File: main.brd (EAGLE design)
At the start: 24.5 x 25.1 mm, 35 parts, among them IC1 ATTINY13A-SSH, IC2 TP4056-42-ESOP8, IC3 LM27313XMFX_NOPB, T1A 2N4401, T1B NPN, X1 MINI-USB-UX60A-MB-5ST

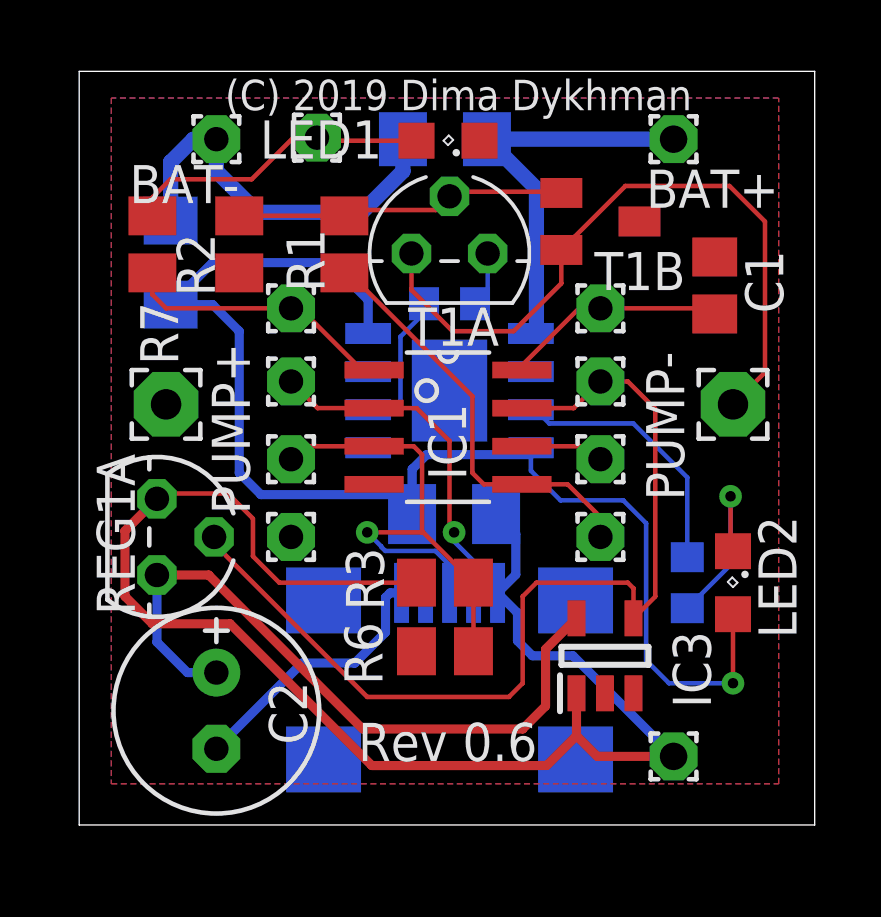
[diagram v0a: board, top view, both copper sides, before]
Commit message: solar parameters tuned
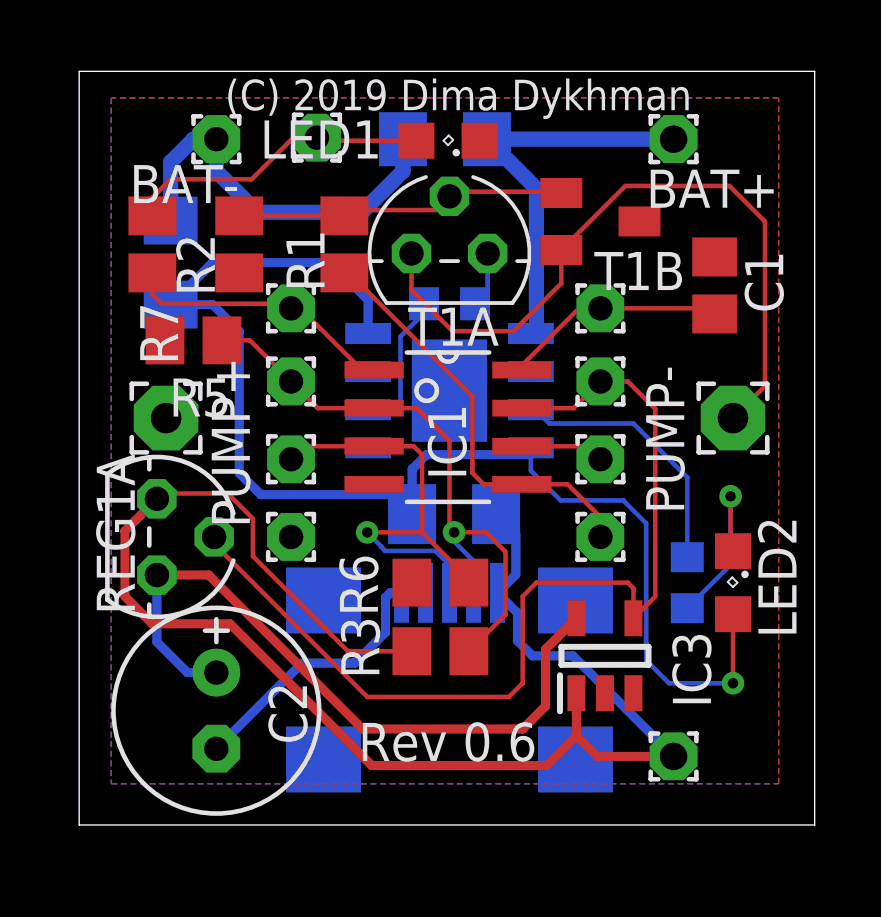
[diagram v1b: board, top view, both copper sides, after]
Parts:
- added R5: 10k, resistor:M0805
- moved R3 2.29 mm to (13.0, 5.94)
- moved R6 2.29 mm to (13.0, 8.23)
- moved PUMP+ 0.46 mm to (3.81, 13.7)
- moved PUMP- 0.46 mm to (22.7, 13.7)
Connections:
- net GND: now also R5.2
- net SENSOR-: no longer R3.1
- net UART_TX: now also R3.1, R5.1
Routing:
- net UART_TX: track 11.5 -> 20.2 mm
- net SENSOR-: track 17.9 -> 15.5 mm
- net N$3: track 48.9 -> 49.7 mm
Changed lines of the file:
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@@
 <attribute name="VALUE" x="8.7884" y="18.2372" size="1.27" layer="27" rot="R90"/>
 </element>
-<element name="PUMP-" library="wirepad" library_urn="urn:adsk.eagle:library:412" package="2,15/1,0" package3d_urn="urn:adsk.eagle:package:30831/1" value="" x="22.7076" y="14.1732" smashed="yes" rot="R90">
-<attribute name="NAME" x="21.082" y="10.9728" size="1.27" layer="25" ratio="10" rot="R90"/>
-<attribute name="VALUE" x="22.1076" y="14.1732" size="0.0254" layer="27" rot="R90"/>
-</element>
-<element name="PUMP+" library="wirepad" library_urn="urn:adsk.eagle:library:412" package="2,15/1,0" package3d_urn="urn:adsk.eagle:package:30831/1" value="" x="3.81" y="14.1732" smashed="yes" rot="R90">
-<attribute name="NAME" x="6.604" y="10.5156" size="1.27" layer="25" ratio="10" rot="R90"/>
-<attribute name="VALUE" x="3.21" y="14.1732" size="0.0254" layer="27" rot="R90"/>
+<element name="PUMP-" library="wirepad" library_urn="urn:adsk.eagle:library:412" package="2,15/1,0" package3d_urn="urn:adsk.eagle:package:30831/1" value="" x="22.7076" y="13.716" smashed="yes" rot="R90">
+<attribute name="NAME" x="21.082" y="10.5156" size="1.27" layer="25" ratio="10" rot="R90"/>
+<attribute name="VALUE" x="22.1076" y="13.716" size="0.0254" layer="27" rot="R90"/>
+</element>
+<element name="PUMP+" library="wirepad" library_urn="urn:adsk.eagle:library:412" package="2,15/1,0" package3d_urn="urn:adsk.eagle:package:30831/1" value="" x="3.81" y="13.716" smashed="yes" rot="R90">
+<attribute name="NAME" x="6.604" y="10.0584" size="1.27" layer="25" ratio="10" rot="R90"/>
+<attribute name="VALUE" x="3.21" y="13.716" size="0.0254" layer="27" rot="R90"/>
 </element>
 <element name="PAD1" library="wirepad" library_urn="urn:adsk.eagle:library:412" package="1,6/0,8" package3d_urn="urn:adsk.eagle:package:30830/1" value="" x="8.8392" y="23.0632" smashed="yes">
@@
 <attribute name="VALUE" x="2.2352" y="6.8326" size="1.27" layer="27" ratio="10" rot="R270"/>
 </element>
-<element name="R6" library="resistor" library_urn="urn:adsk.eagle:library:348" package="M0805" package3d_urn="urn:adsk.eagle:package:23556/1" value="10k" x="13.1064" y="5.9436" smashed="yes" rot="R180">
-<attribute name="NAME" x="11.0236" y="4.826" size="1.27" layer="25" rot="R90"/>
-<attribute name="VALUE" x="14.3764" y="8.4836" size="1.27" layer="27" rot="R180"/>
+<element name="R6" library="resistor" library_urn="urn:adsk.eagle:library:348" package="M0805" package3d_urn="urn:adsk.eagle:package:23556/1" value="10k" x="12.954" y="8.2296" smashed="yes" rot="R180">
+<attribute name="NAME" x="10.8712" y="7.112" size="1.27" layer="25" rot="R90"/>
+<attribute name="VALUE" x="14.224" y="10.7696" size="1.27" layer="27" rot="R180"/>
 </element>
 <element name="C1" library="rcl" library_urn="urn:adsk.eagle:library:334" package="C0805" package3d_urn="urn:adsk.eagle:package:23617/2" value="100nF" x="22.098" y="18.1356" smashed="yes" rot="R90">
@@
 <attribute name="VALUE" x="24.638" y="16.8656" size="1.27" layer="27" rot="R90"/>
 </element>
-<element name="R3" library="resistor" library_urn="urn:adsk.eagle:library:348" package="M0805" package3d_urn="urn:adsk.eagle:package:23556/1" value="10k" x="13.1064" y="8.2296" smashed="yes" rot="R180">
-<attribute name="NAME" x="9.8044" y="9.398" size="1.27" layer="25" rot="R270"/>
-<attribute name="VALUE" x="14.3764" y="10.7696" size="1.27" layer="27" rot="R180"/>
+<element name="R3" library="resistor" library_urn="urn:adsk.eagle:library:348" package="M0805" package3d_urn="urn:adsk.eagle:package:23556/1" value="10k" x="12.954" y="5.9436" smashed="yes" rot="R180">
+<attribute name="NAME" x="9.652" y="7.112" size="1.27" layer="25" rot="R270"/>
+<attribute name="VALUE" x="14.224" y="8.4836" size="1.27" layer="27" rot="R180"/>
 </element>
 <element name="R7" library="resistor" library_urn="urn:adsk.eagle:library:348" package="M0805" package3d_urn="urn:adsk.eagle:package:23556/1" value="510" x="3.3528" y="19.5072" smashed="yes" rot="R90">
@@
 <attribute name="RS_PRICE-STOCK" value="" x="18.4404" y="5.7912" size="1.778" layer="27" rot="R90" display="off"/>
 <attribute name="VALUE" x="18.4404" y="5.7912" size="1.27" layer="27" rot="R90" align="center"/>
+</element>
+<element name="R5" library="resistor" library_urn="urn:adsk.eagle:library:348" package="M0805" package3d_urn="urn:adsk.eagle:package:23556/1" value="10k" x="4.7244" y="16.3068" smashed="yes" rot="R180">
+<attribute name="NAME" x="5.9944" y="15.0368" size="1.27" layer="25" rot="R180"/>
+<attribute name="VALUE" x="5.9944" y="18.8468" size="1.27" layer="27" rot="R180"/>
 </element>
 </elements>
@@
 <contactref element="X1" pad="2"/>
 <wire x1="14.0588" y1="8.9536" x2="14.0588" y2="7.8888" width="0.1524" layer="16"/>
+<contactref element="R5" pad="1"/>
+<contactref element="R3" pad="1"/>
+<wire x1="5.6744" y1="16.3068" x2="6.604" y2="16.3068" width="0.1524" layer="1"/>
+<wire x1="6.604" y1="16.3068" x2="7.9756" y2="14.9352" width="0.1524" layer="1"/>
+<wire x1="15.1232" y1="9.2608" x2="14.478" y2="9.906" width="0.1524" layer="1"/>
+<wire x1="13.4112" y1="9.906" x2="14.478" y2="9.906" width="0.1524" layer="1"/>
+<wire x1="15.1232" y1="9.2608" x2="15.1232" y2="7.1628" width="0.1524" layer="1"/>
+<wire x1="15.1232" y1="7.1628" x2="13.904" y2="5.9436" width="0.1524" layer="1"/>
 </signal>
 <signal name="GND">
@@
 <wire x1="8.3422" y1="5.5482" x2="5.4864" y2="2.6924" width="0.3048" layer="16"/>
 <contactref element="IC3" pad="2"/>
+<contactref element="R5" pad="2"/>
 </signal>
 <signal name="N$1">
@@
 <contactref element="T1B" pad="2"/>
 <contactref element="PUMP-" pad="1"/>
-<wire x1="22.7076" y1="14.1732" x2="23.7744" y2="15.24" width="0.1524" layer="1"/>
-<wire x1="23.7744" y1="15.24" x2="23.7744" y2="20.2692" width="0.1524" layer="1"/>
+<wire x1="22.7076" y1="13.716" x2="23.7744" y2="14.7828" width="0.1524" layer="1"/>
+<wire x1="23.7744" y1="14.7828" x2="23.7744" y2="20.2692" width="0.1524" layer="1"/>
 <wire x1="23.7744" y1="20.2692" x2="22.5908" y2="21.4528" width="0.1524" layer="1"/>
 <wire x1="22.5908" y1="21.4528" x2="19.1186" y2="21.4528" width="0.1524" layer="1"/>
@@
 <wire x1="10.7442" y1="15.3162" x2="10.3378" y2="15.3162" width="0.1524" layer="1"/>
 <contactref element="R7" pad="1"/>
-<wire x1="3.81" y1="17.3736" x2="3.3528" y2="17.8308" width="0.1524" layer="1"/>
+<wire x1="3.6576" y1="17.526" x2="3.3528" y2="17.8308" width="0.1524" layer="1"/>
 <wire x1="3.3528" y1="18.5572" x2="3.3528" y2="17.8308" width="0.1524" layer="1"/>
-<wire x1="3.81" y1="17.3736" x2="7.9756" y2="17.3736" width="0.1524" layer="1"/>
+<wire x1="7.8232" y1="17.526" x2="3.6576" y2="17.526" width="0.1524" layer="1"/>
+<wire x1="7.8232" y1="17.526" x2="7.9756" y2="17.3736" width="0.1524" layer="1"/>
 </signal>
 <signal name="SENSOR-">
@@
 <contactref element="PAD8" pad="1"/>
 <contactref element="R6" pad="1"/>
-<contactref element="R3" pad="1"/>
 <wire x1="10.7442" y1="12.7762" x2="8.4074" y2="12.7762" width="0.1524" layer="1"/>
 <wire x1="8.4074" y1="12.7762" x2="7.9756" y2="12.3444" width="0.1524" layer="1"/>
@@
 <wire x1="10.9826" y1="9.439" x2="10.5156" y2="9.906" width="0.1524" layer="16"/>
 <wire x1="12.7862875" y1="9.287" x2="11.1165125" y2="9.287" width="0.1524" layer="16"/>
-<wire x1="14.0564" y1="5.9436" x2="14.0564" y2="8.2296" width="0.1524" layer="1"/>
-<wire x1="12.3444" y1="9.906" x2="12.38" y2="9.906" width="0.1524" layer="1"/>
-<wire x1="12.38" y1="9.906" x2="14.0564" y2="8.2296" width="0.1524" layer="1"/>
 <contactref element="X1" pad="3"/>
 <wire x1="13.2588" y1="8.8144875" x2="13.2588" y2="7.8888" width="0.1524" layer="16"/>
 <wire x1="12.7862875" y1="9.287" x2="13.2588" y2="8.8144875" width="0.1524" layer="16"/>
+<wire x1="13.904" y1="8.2296" x2="13.904" y2="8.3464" width="0.1524" layer="1"/>
+<wire x1="13.904" y1="8.3464" x2="12.3444" y2="9.906" width="0.1524" layer="1"/>
 </signal>
 <signal name="N$6">
@@
 <wire x1="16.0235125" y1="5.7912" x2="17.3736" y2="5.7912" width="0.3048" layer="16"/>
 <wire x1="20.7264" y1="2.4384" x2="17.3736" y2="5.7912" width="0.3048" layer="16"/>
-<wire x1="6.7056" y1="9.1084" x2="7.5844" y2="8.2296" width="0.1524" layer="1"/>
-<wire x1="7.5844" y1="8.2296" x2="12.1564" y2="8.2296" width="0.1524" layer="1"/>
+<wire x1="6.7056" y1="9.1084" x2="9.8704" y2="5.9436" width="0.1524" layer="1"/>
+<wire x1="9.8704" y1="5.9436" x2="12.004" y2="5.9436" width="0.1524" layer="1"/>
 <contactref element="IC3" pad="1"/>
 <wire x1="16.4956" y1="2.1336" x2="17.4904" y2="3.1284" width="0.3048" layer="1"/>

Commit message: new graphics
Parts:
- removed BAT+: (no value), wirepad:1,6/0,9
- added X2: 332-02, con-garry:332-02
- moved PAD1 0.76 mm to (9.60, 23.0)
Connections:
- net VCC: now also X2.1; no longer BAT+.1
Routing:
- net VCC: track 20.9 -> 14.7 mm
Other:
- board size 24.5 x 25.1 mm -> 24.4 x 26.2 mm
- board text added: "(C) 2020 Dima Dykhman"
- board text removed: "(C) 2019 Dima Dykhman"

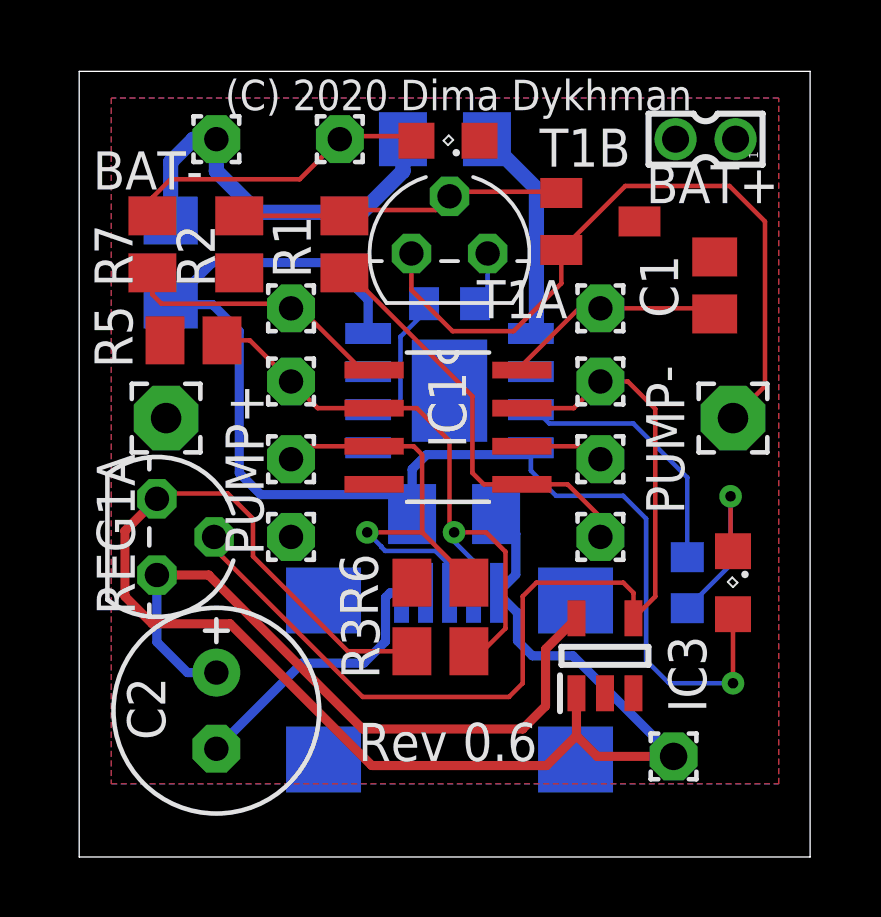
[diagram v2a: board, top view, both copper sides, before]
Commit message: removed bootloader added USBasp
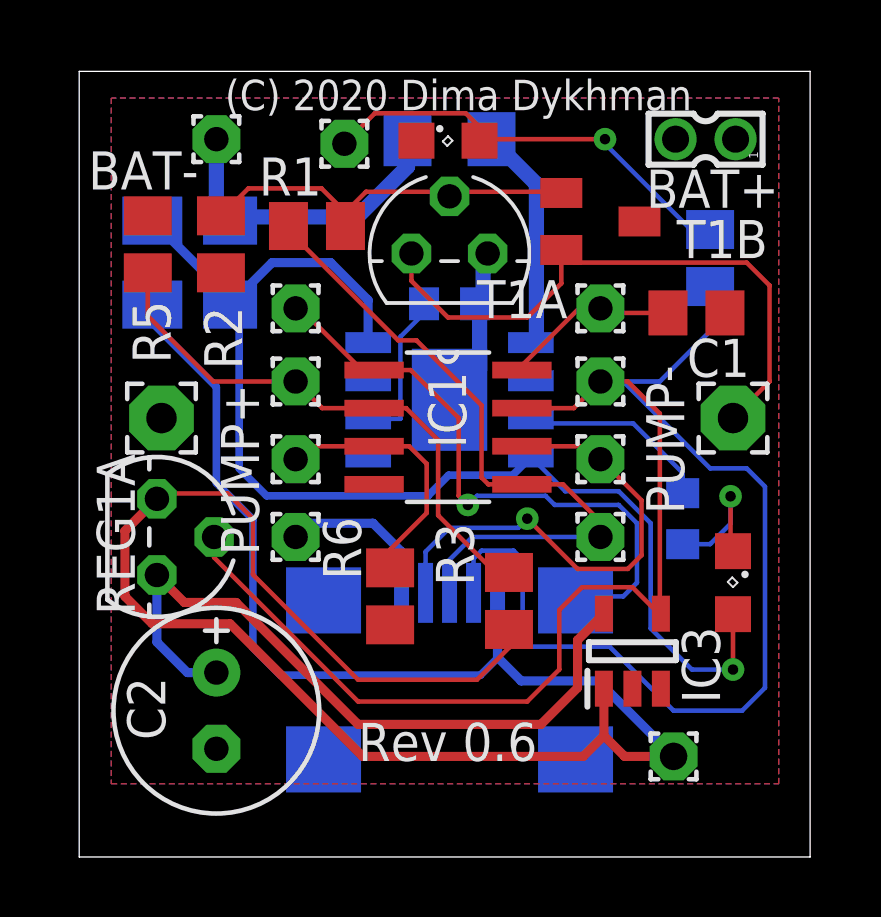
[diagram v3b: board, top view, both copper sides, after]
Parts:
- moved R7 18.6 mm to (21.9, 19.1), flipped to the bottom
- moved R4 13.1 mm to (3.35, 18.9), turned to 90 degrees
- moved R5 3.54 mm to (3.20, 19.5), turned to 90 degrees
- moved R3 2.83 mm to (15.2, 7.62), turned to 270 degrees
- moved R8 2.14 mm to (21.0, 10.4)
- moved C3 1.98 mm to (5.94, 18.9)
- moved R6 1.74 mm to (11.3, 7.77), turned to 270 degrees
- moved C1 1.10 mm to (21.5, 17.2), turned to 0 degrees
- moved R1 1.10 mm to (8.84, 20.1), turned to 180 degrees
- moved IC3 0.93 mm to (19.4, 5.94)
- moved R2 0.61 mm to (5.64, 19.5)
- moved IC2 0.30 mm to (13.3, 14.3)
- moved PAD1 0.22 mm to (9.75, 22.9)
- moved C4 0.15 mm to (13.3, 23.0)
- moved PAD10 0.15 mm to (8.13, 17.4)
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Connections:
- removed net LED: IC1.1, PAD10.1, R7.1
- new net RESET: IC1.1, PAD10.1
- net GND: now also IC2.9
- net PUMP: now also X1.3
- net SENSOR+: now also X1.4
- net SENSOR-: no longer X1.3
- net SOLAR: now also R7.1, X1.2
- net UART_TX: no longer X1.2
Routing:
- net SOLAR: track 33.1 -> 67.3 mm
- net N$3: track 49.7 -> 76.0 mm
- net RESET: track 0.00 -> 19.9 mm, vias 0 -> 1
- net SENSOR+: track 2.86 -> 16.5 mm, vias 0 -> 1
- net LED: track 9.16 -> 0.00 mm
- net PUMP: track 14.1 -> 22.9 mm
- net SENSOR-: track 15.5 -> 8.76 mm, vias 1 -> 0
- net N$6: track 10.3 -> 14.6 mm, vias 0 -> 1
- net N$2: track 23.7 -> 20.4 mm
- net GND: track 24.8 -> 21.5 mm
- net N$4: track 43.7 -> 40.8 mm
- net N$8: track 8.80 -> 6.48 mm
- net UART_TX: track 20.4 -> 18.5 mm, vias 1 -> 0
- net N$1: track 11.1 -> 12.9 mm
- net N$9: track 6.19 -> 4.65 mm
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
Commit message: improved solar
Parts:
- added IC4: TPL5110DDCT, SamacSys:SOT95P280X110-6N
- added R10: 100k, resistor:M0805
- moved IC3 8.25 mm to (11.4, 3.66), turned to 180 degrees
- moved R8 4.44 mm to (22.7, 6.25), turned to 270 degrees
- moved LED2 2.85 mm to (23.5, 5.49)
- moved R3 1.23 mm to (14.2, 8.23)
- moved R6 0.48 mm to (11.1, 8.23)
- moved LED1 0.15 mm to (13.4, 23.0)
- moved PAD1 0.15 mm to (9.75, 23.0)
- moved T1B 0.15 mm to (18.4, 20.3)
- moved C4 0.15 mm to (13.4, 23.0)
- moved T1A 0.15 mm to (13.4, 19.2)
- turned C1 to 180 degrees
- turned IN+ to 90 degrees
- renumbered BAT- to B-
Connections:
- new net N$3: C1.2, IC1.8, IC4.5, PAD3.1
- new net N$7: IC4.3, R10.1
- net GND: now also C1.1, IC4.2, R10.2; no longer C1.2
- net SOLAR: now also IC4.4
- net VCC: now also IC4.1, IC4.6; no longer C1.1, IC1.8, PAD3.1
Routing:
- net N$3: track 0.00 -> 22.4 mm
- net N$5: track 76.0 -> 62.0 mm
- net SOLAR_PANEL+: track 24.1 -> 14.5 mm
- net N$8: track 6.48 -> 13.4 mm
- net N$7: track 0.00 -> 2.87 mm
- net VCC: track 13.3 -> 11.5 mm, vias 0 -> 1
- net N$4: track 40.8 -> 42.3 mm
- net UART_TX: track 18.5 -> 17.2 mm
- net N$9: track 4.65 -> 5.25 mm
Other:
- board text added: "B+"
- board text added: "B-"
- board text added: "P+"
- board text added: "P-"
- board text added: "Rev 0.7"
- board text removed: "BAT+"
- board text removed: "BAT-"
- board text removed: "Rev 0.6"

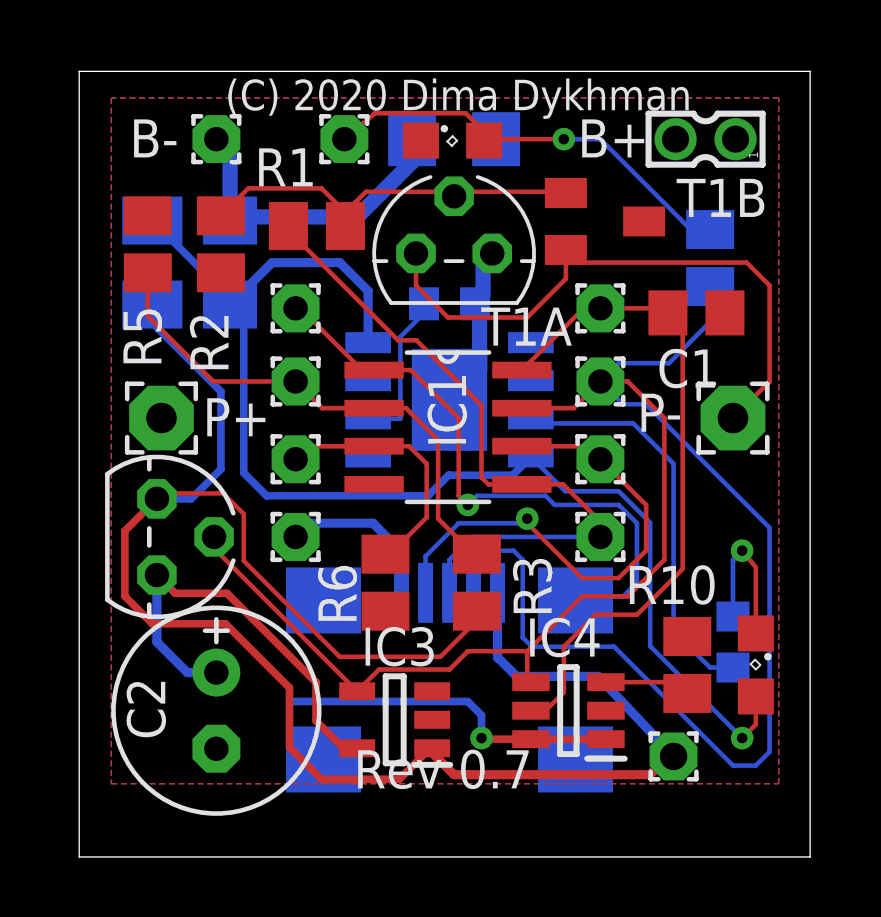
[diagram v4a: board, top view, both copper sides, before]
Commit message: remapped LED gpio
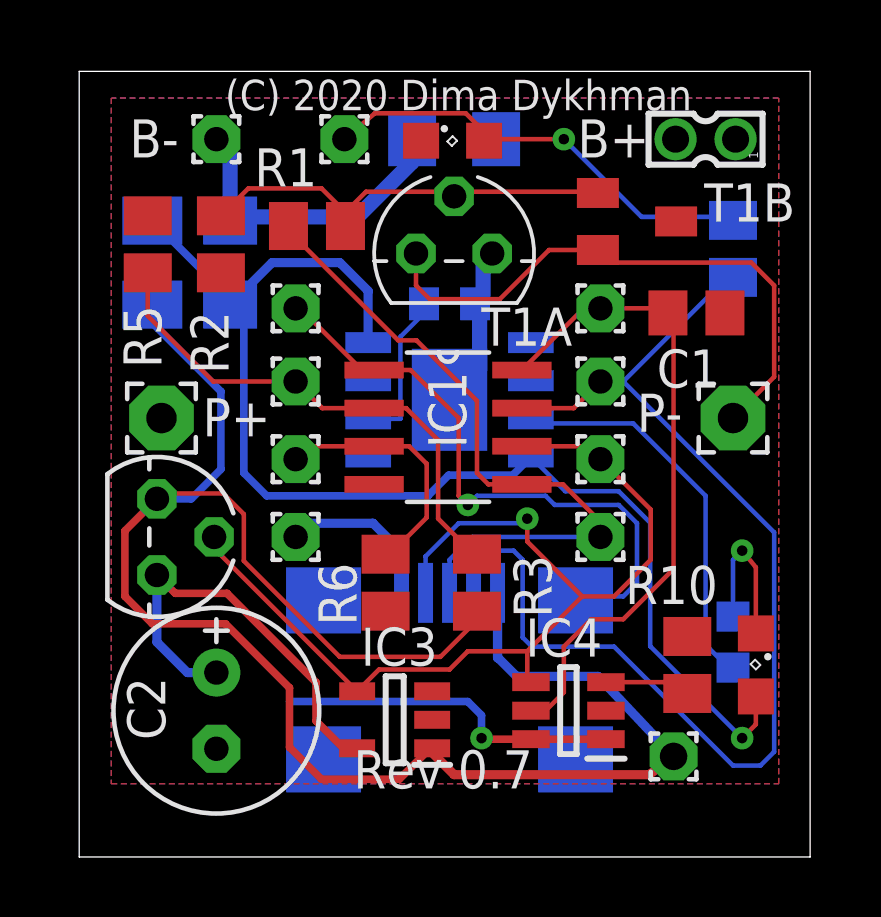
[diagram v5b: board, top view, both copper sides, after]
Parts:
- moved T1B 1.07 mm to (19.5, 20.3)
- moved R7 0.82 mm to (22.7, 19.4)
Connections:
- net PUMP renamed SENSOR/PUMP
- removed net SENSOR+: IC1.6, PAD6.1, X1.4
- new net LED: IC1.7, PAD4.1, R7.1, X1.2
- net SOLAR: now also IC1.6, PAD6.1, X1.4; no longer IC1.7, PAD4.1, R7.1, X1.2
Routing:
- net LED: track 0.00 -> 39.2 mm
- net SOLAR: track 67.3 -> 35.2 mm, vias 0 -> 1
- net SENSOR+: track 16.9 -> 0.00 mm, vias 1 -> 0
- net N$1: track 13.1 -> 14.2 mm
- net N$2: track 20.2 -> 19.4 mm
- net N$6: track 14.3 -> 15.0 mm
